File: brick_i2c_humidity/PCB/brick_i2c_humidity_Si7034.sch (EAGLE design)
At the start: 16 parts

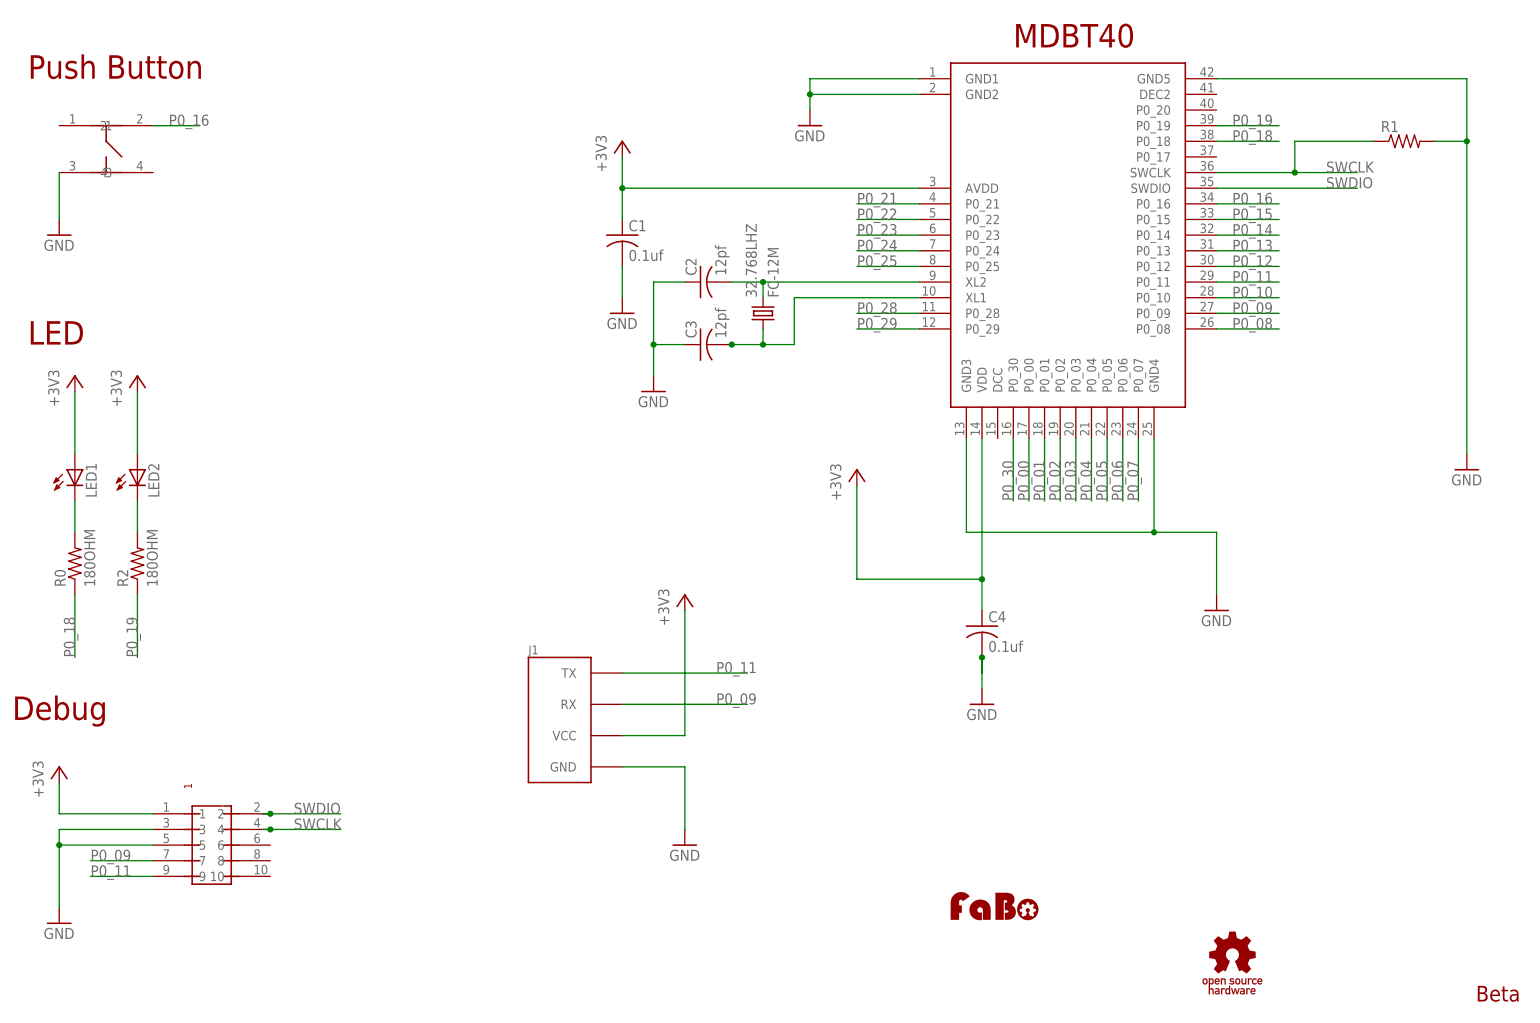
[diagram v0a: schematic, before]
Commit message: Delete unused file
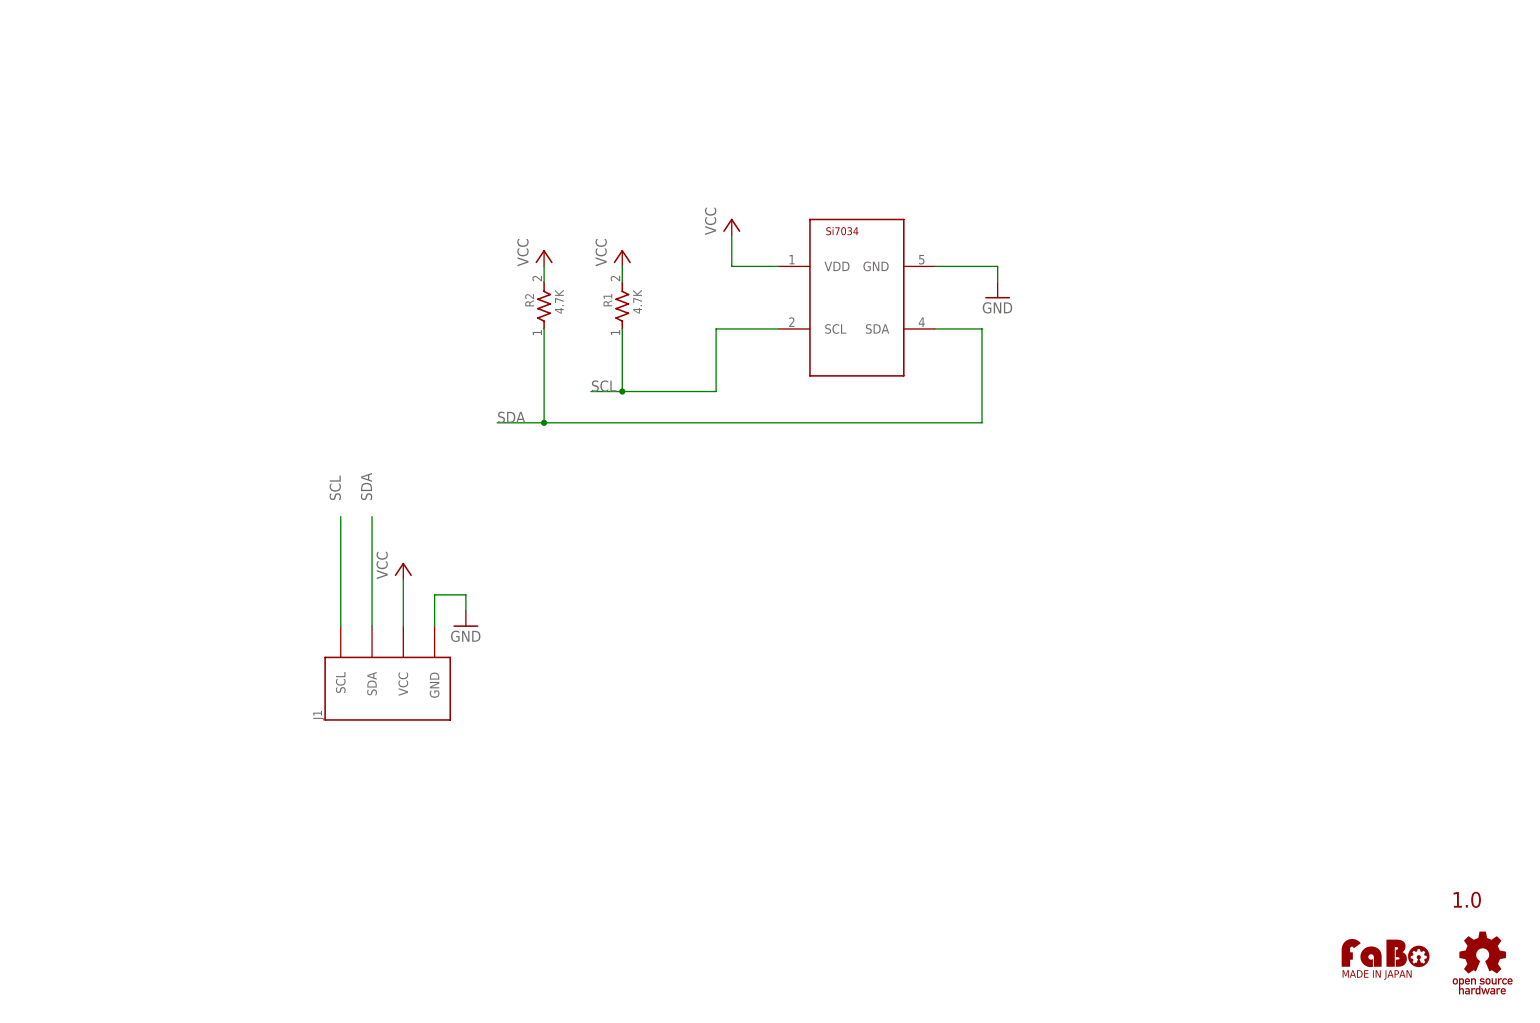
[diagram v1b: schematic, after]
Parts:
- removed 32.768LHZ: FC-12M, crystal:FC-12M
- removed C1, C4: 0.1uf, adafruit:C-USC0603
- removed C2, C3: 12pf, adafruit:C-USC0603
- removed LED1, LED2: (no value), led:LEDCHIP-LED0603
- removed R0: 180OHM, SparkFun:RESISTOR0603-RES
- removed U$1: RAYTAC-MDBT40, gclueBT:RAYTAC-MDBT40
- removed U$5: SWICTH-4P(KMR2), gclue-test:SWICTH-4P(KMR2)
- J1: device gclue:BRICK_SERIAL -> gclue:BRICK_I2C
- R1: value (none) -> 4.7K; device adafruit:R-US_R0603 -> GClue-Resistors:RESISTOR0603
- R2: value 180OHM -> 4.7K; device SparkFun:RESISTOR0603-RES -> GClue-Resistors:RESISTOR0603
- U$2: value PIN-HEADER-SMT(1.27MM)2X5 -> (none); device gclue:PIN-HEADER-SMT(1.27MM)2X5 -> FaBo:LOGO_FABO-M
- U$3: value (none) -> SILICONLABS-SI7034; device FaBo:LOGO_FABO-S -> FaBo-Mems:SILICONLABS-SI7034
- U$4: device gclue:LOGO_OSHW_T-S -> gclue:LOGO_OSHW_T-M
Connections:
- removed net +3V3: C1.1, C4.1, J1.VCC, LED1.A, LED2.A, U$1.AVDD, U$1.VDD, U$2.1
- removed net LED1: LED1.C, R0.2
- removed net N$2: LED2.C, R2.2
- removed net N$7: 32.768LHZ.2, C2.2, U$1.XL2
- removed net N$8: 32.768LHZ.1, C3.2, U$1.XL1
- removed net P0_00: U$1.P0_00
- removed net P0_01: U$1.P0_01
- removed net P0_02: U$1.P0_02
- removed net P0_03: U$1.P0_03
- removed net P0_04: U$1.P0_04
- removed net P0_05: U$1.P0_05
- removed net P0_06: U$1.P0_06
- removed net P0_07: U$1.P0_07
- removed net P0_08: U$1.P0_08
- removed net P0_09: J1.RX, U$1.P0_09, U$2.7
- removed net P0_10: U$1.P0_10
- removed net P0_11: J1.TX, U$1.P0_11, U$2.9
- removed net P0_12: U$1.P0_12
- removed net P0_13: U$1.P0_13
- removed net P0_14: U$1.P0_14
- removed net P0_15: U$1.P0_15
- removed net P0_16: U$1.P0_16, U$5.2
- removed net P0_18: R0.1, U$1.P0_18
- removed net P0_19: R2.1, U$1.P0_19
- removed net P0_21: U$1.P0_21
- removed net P0_22: U$1.P0_22
- removed net P0_23: U$1.P0_23
- removed net P0_24: U$1.P0_24
- removed net P0_25: U$1.P0_25
- removed net P0_28: U$1.P0_28
- removed net P0_29: U$1.P0_29
- removed net P0_30: U$1.P0_30
- removed net SWCLK: R1.1, U$1.SWCLK, U$2.4
- removed net SWDIO: U$1.SWDIO, U$2.2
- new net SCL: J1.SCL, R1.1, U$3.SCL
- new net SDA: J1.SDA, R2.1, U$3.SDA
- new net VCC: J1.VCC, R1.2, R2.2, U$3.VDD
- net GND: now also U$3.GND; no longer C1.2, C2.1, C3.1, C4.2, R1.2, U$1.GND1, U$1.GND2, U$1.GND3, U$1.GND4, U$1.GND5, U$2.3, U$2.5, U$5.3
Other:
- note added: "1.0"
- note removed: "Beta"
- note removed: "Debug"
- note removed: "LED"
- note removed: "MDBT40"
- note removed: "Push Button"
- moved on the sheet: J1, R1, R2

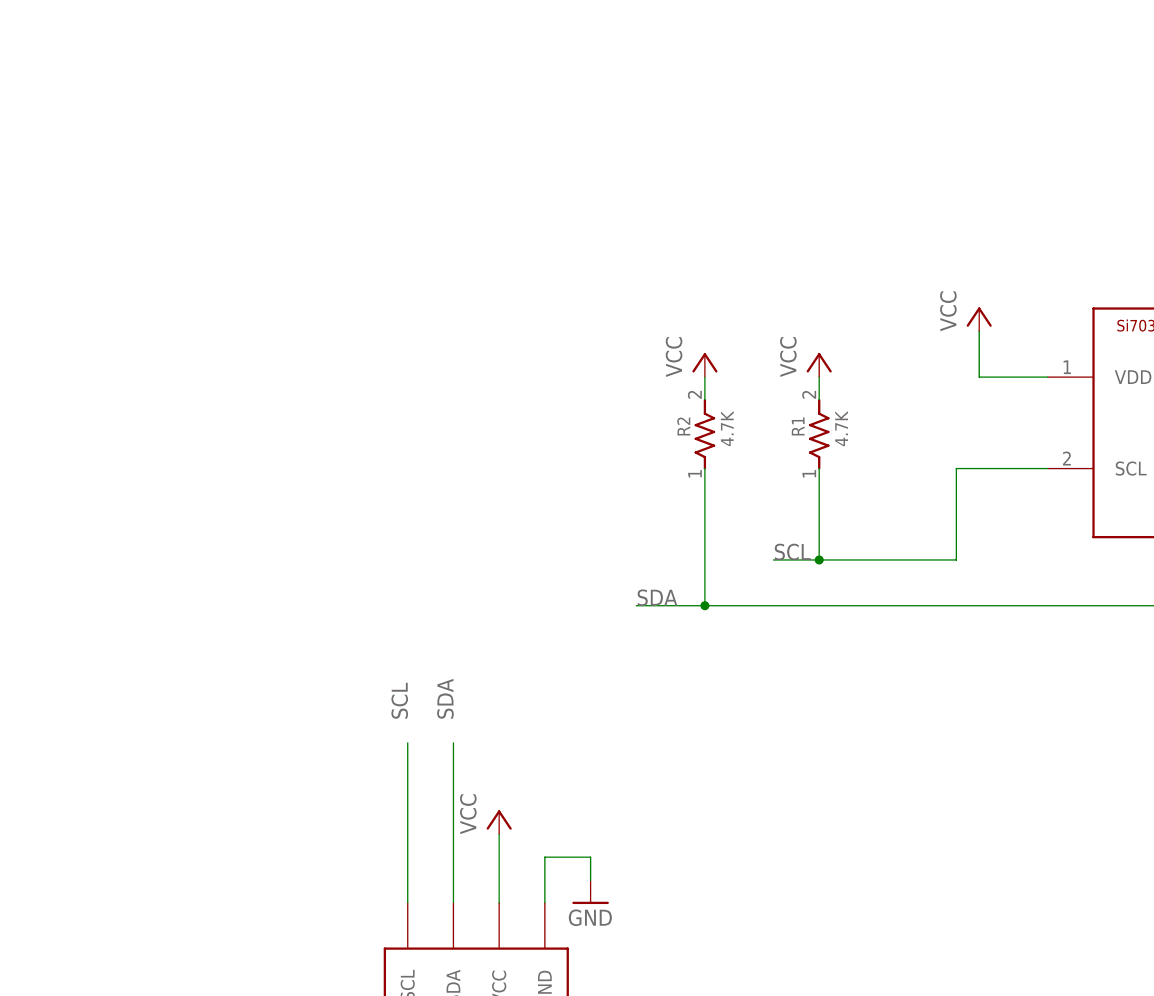
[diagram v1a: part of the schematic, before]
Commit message: Update Si7034
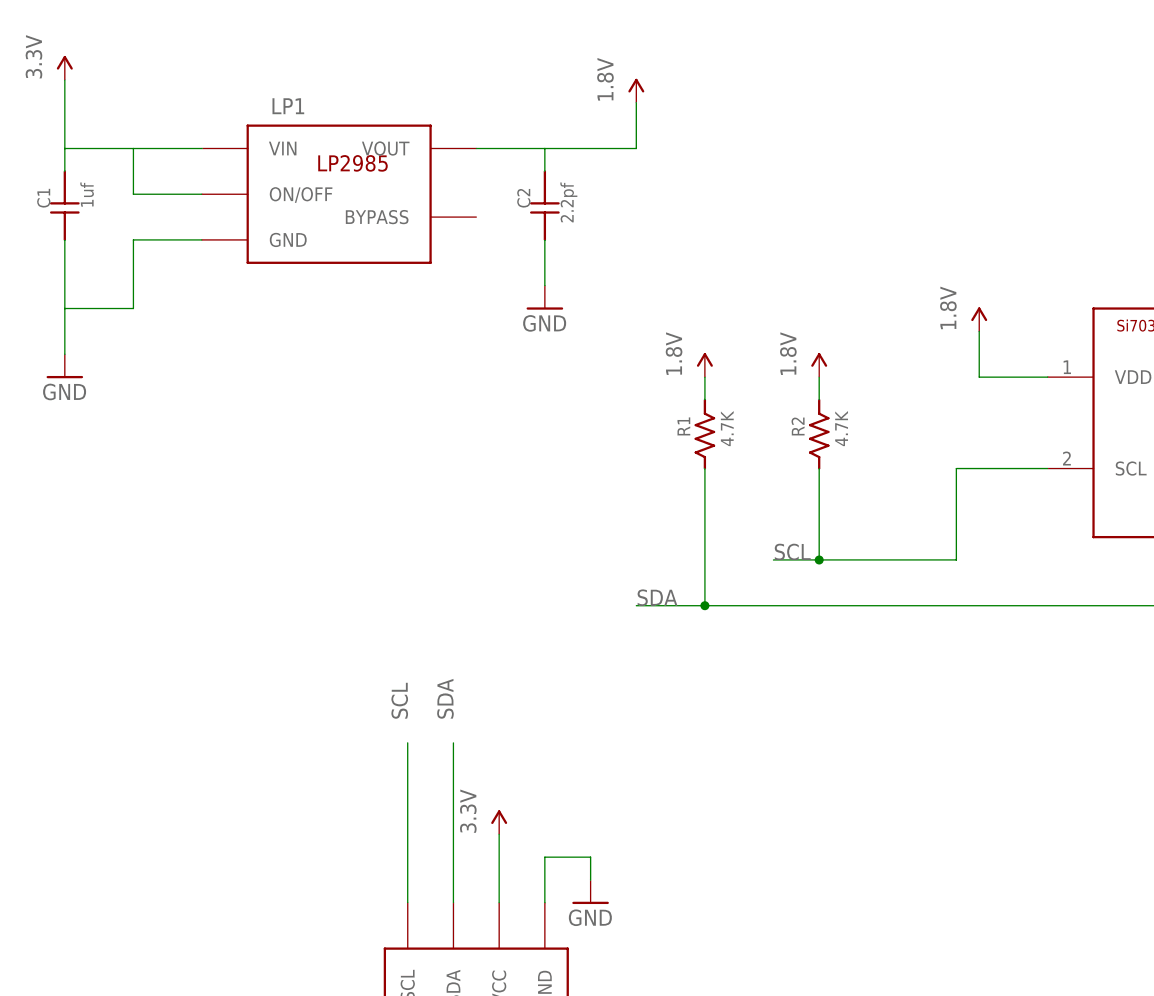
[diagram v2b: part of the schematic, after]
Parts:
- added C1: 1uf, FaBo-Capacitor:CAPACITOR0603
- added C2: 2.2pf, FaBo-Capacitor:CAPACITOR0603
- added LP1: (no value), FaBo-Supply:TI-LP2985-18DBVT
- R1, R2: device GClue-Resistors:RESISTOR0603 -> FaBo-Resistors:RESISTOR-0603
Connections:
- removed net VCC: J1.VCC, R1.2, R2.2, U$3.VDD
- new net 1.8V: C2.2, LP1.VOUT, R1.2, R2.2, U$3.VDD
- new net 3.3V: C1.2, J1.VCC, LP1.ON/OFF, LP1.VIN
- net GND: now also C1.1, C2.1, LP1.GND
- net SCL: now also R2.1; no longer R1.1
- net SDA: now also R1.1; no longer R2.1
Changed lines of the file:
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@@
 <parts>
 <part name="U$1" library="gclue" deviceset="A4L-LOC" device=""/>
-<part name="P+1" library="supply1" deviceset="VCC" device=""/>
-<part name="P+2" library="supply1" deviceset="VCC" device=""/>
-<part name="P+3" library="supply1" deviceset="VCC" device=""/>
 <part name="GND1" library="supply1" deviceset="GND" device=""/>
 <part name="GND2" library="supply1" deviceset="GND" device=""/>
 <part name="J1" library="gclue" deviceset="BRICK_I2C" device=""/>
-<part name="R2" library="GClue-Resistors" deviceset="RESISTOR" device="0603" value="4.7K"/>
-<part name="R1" library="GClue-Resistors" deviceset="RESISTOR" device="0603" value="4.7K"/>
 <part name="U$4" library="gclue" deviceset="LOGO_OSHW_T" device="-M"/>
 <part name="U$2" library="FaBo" deviceset="LOGO_FABO" device="-M"/>
 <part name="U$3" library="FaBo-Mems" deviceset="SILICONLABS-SI7034" device=""/>
-<part name="P+4" library="supply1" deviceset="VCC" device=""/>
+<part name="+1.8V1" library="FaBo-Supply" deviceset="1.8V" device=""/>
+<part name="3.3V1" library="FaBo-Supply" deviceset="3.3V" device=""/>
+<part name="+1.8V2" library="FaBo-Supply" deviceset="1.8V" device=""/>
+<part name="+1.8V3" library="FaBo-Supply" deviceset="1.8V" device=""/>
+<part name="+1.8V4" library="FaBo-Supply" deviceset="1.8V" device=""/>
+<part name="3.3V2" library="FaBo-Supply" deviceset="3.3V" device=""/>
+<part name="R1" library="FaBo-Resistors" deviceset="RESISTOR" device="-0603" value="4.7K"/>
+<part name="R2" library="FaBo-Resistors" deviceset="RESISTOR" device="-0603" value="4.7K"/>
+<part name="LP1" library="FaBo-Supply" deviceset="TI-LP2985" device="-18DBVT"/>
+<part name="GND3" library="supply1" deviceset="GND" device=""/>
+<part name="C1" library="FaBo-Capacitor" deviceset="CAPACITOR" device="0603" value="1uf"/>
+<part name="GND4" library="supply1" deviceset="GND" device=""/>
+<part name="C2" library="FaBo-Capacitor" deviceset="CAPACITOR" device="0603" value="2.2pf"/>
 </parts>
 <sheets>
@@
 <instances>
 <instance part="U$1" gate="G$1" x="0" y="0"/>
-<instance part="P+1" gate="VCC" x="73.66" y="76.2"/>
-<instance part="P+2" gate="VCC" x="109.22" y="127"/>
-<instance part="P+3" gate="VCC" x="96.52" y="127"/>
 <instance part="GND1" gate="1" x="83.82" y="66.04"/>
 <instance part="GND2" gate="1" x="170.18" y="119.38"/>
 <instance part="J1" gate="G$1" x="71.12" y="58.42" rot="R90"/>
-<instance part="R2" gate="G$1" x="96.52" y="116.84" rot="R90"/>
-<instance part="R1" gate="G$1" x="109.22" y="116.84" rot="R90"/>
 <instance part="U$4" gate="G$1" x="248.92" y="12.7"/>
 <instance part="U$2" gate="G$1" x="226.06" y="15.24"/>
 <instance part="U$3" gate="G$1" x="147.32" y="119.38"/>
-<instance part="P+4" gate="VCC" x="127" y="132.08"/>
+<instance part="+1.8V1" gate="G$1" x="88.9" y="154.94"/>
+<instance part="3.3V1" gate="G$1" x="25.4" y="157.48"/>
+<instance part="+1.8V2" gate="G$1" x="96.52" y="124.46"/>
+<instance part="+1.8V3" gate="G$1" x="109.22" y="124.46"/>
+<instance part="+1.8V4" gate="G$1" x="127" y="129.54"/>
+<instance part="3.3V2" gate="G$1" x="73.66" y="73.66"/>
+<instance part="R1" gate="G$1" x="96.52" y="116.84" rot="R90"/>
+<instance part="R2" gate="G$1" x="109.22" y="116.84" rot="R90"/>
+<instance part="LP1" gate="G$1" x="55.88" y="144.78"/>
+<instance part="GND3" gate="1" x="25.4" y="124.46"/>
+<instance part="C1" gate="G$1" x="25.4" y="142.24" rot="R90"/>
+<instance part="GND4" gate="1" x="78.74" y="132.08"/>
+<instance part="C2" gate="G$1" x="78.74" y="142.24" rot="R90"/>
 </instances>
 <busses>
@@
 <junction x="96.52" y="99.06"/>
 <label x="88.9" y="99.06" size="1.778" layer="95"/>
-<pinref part="R2" gate="G$1" pin="1"/>
 <wire x1="160.02" y1="114.3" x2="167.64" y2="114.3" width="0.1524" layer="91"/>
 <wire x1="167.64" y1="114.3" x2="167.64" y2="99.06" width="0.1524" layer="91"/>
 <pinref part="U$3" gate="G$1" pin="SDA"/>
+<pinref part="R1" gate="G$1" pin="1"/>
 </segment>
 <segment>
@@
 <label x="68.58" y="86.36" size="1.778" layer="95" rot="R90"/>
 <pinref part="J1" gate="G$1" pin="SDA"/>
-</segment>
-</net>
-<net name="VCC" class="0">
-<segment>
-<pinref part="P+2" gate="VCC" pin="VCC"/>
-<wire x1="109.22" y1="121.92" x2="109.22" y2="124.46" width="0.1524" layer="91"/>
-<pinref part="R1" gate="G$1" pin="2"/>
-</segment>
-<segment>
-<pinref part="P+3" gate="VCC" pin="VCC"/>
-<wire x1="96.52" y1="121.92" x2="96.52" y2="124.46" width="0.1524" layer="91"/>
-<pinref part="R2" gate="G$1" pin="2"/>
-</segment>
-<segment>
-<pinref part="P+1" gate="VCC" pin="VCC"/>
-<wire x1="73.66" y1="66.04" x2="73.66" y2="73.66" width="0.1524" layer="91"/>
-<pinref part="J1" gate="G$1" pin="VCC"/>
-</segment>
-<segment>
-<pinref part="U$3" gate="G$1" pin="VDD"/>
-<pinref part="P+4" gate="VCC" pin="VCC"/>
-<wire x1="134.62" y1="124.46" x2="127" y2="124.46" width="0.1524" layer="91"/>
-<wire x1="127" y1="124.46" x2="127" y2="129.54" width="0.1524" layer="91"/>
 </segment>
 </net>
@@
 <junction x="109.22" y="104.14"/>
 <label x="104.14" y="104.14" size="1.778" layer="95"/>
-<pinref part="R1" gate="G$1" pin="1"/>
 <pinref part="U$3" gate="G$1" pin="SCL"/>
+<pinref part="R2" gate="G$1" pin="1"/>
 </segment>
 <segment>
@@
 <pinref part="J1" gate="G$1" pin="GND"/>
 </segment>
+<segment>
+<pinref part="LP1" gate="G$1" pin="GND"/>
+<wire x1="40.64" y1="139.7" x2="33.02" y2="139.7" width="0.1524" layer="91"/>
+<wire x1="33.02" y1="139.7" x2="33.02" y2="132.08" width="0.1524" layer="91"/>
+<pinref part="C1" gate="G$1" pin="1"/>
+<wire x1="33.02" y1="132.08" x2="25.4" y2="132.08" width="0.1524" layer="91"/>
+<wire x1="25.4" y1="132.08" x2="25.4" y2="139.7" width="0.1524" layer="91"/>
+<pinref part="GND3" gate="1" pin="GND"/>
+<wire x1="25.4" y1="132.08" x2="25.4" y2="127" width="0.1524" layer="91"/>
+</segment>
+<segment>
+<pinref part="C2" gate="G$1" pin="1"/>
+<pinref part="GND4" gate="1" pin="GND"/>
+<wire x1="78.74" y1="139.7" x2="78.74" y2="134.62" width="0.1524" layer="91"/>
+</segment>
 </net>
+<net name="3.3V" class="0">
+<segment>
+<pinref part="3.3V1" gate="G$1" pin="3.3V"/>
+<wire x1="25.4" y1="157.48" x2="25.4" y2="149.86" width="0.1524" layer="91"/>
+<wire x1="25.4" y1="149.86" x2="33.02" y2="149.86" width="0.1524" layer="91"/>
+<pinref part="LP1" gate="G$1" pin="VIN"/>
+<pinref part="C1" gate="G$1" pin="2"/>
+<wire x1="33.02" y1="149.86" x2="40.64" y2="149.86" width="0.1524" layer="91"/>
+<wire x1="25.4" y1="149.86" x2="25.4" y2="147.32" width="0.1524" layer="91"/>
+<pinref part="LP1" gate="G$1" pin="ON/OFF"/>
+<wire x1="40.64" y1="144.78" x2="33.02" y2="144.78" width="0.1524" layer="91"/>
+<wire x1="33.02" y1="144.78" x2="33.02" y2="149.86" width="0.1524" layer="91"/>
+</segment>
+<segment>
+<wire x1="73.66" y1="66.04" x2="73.66" y2="73.66" width="0.1524" layer="91"/>
+<pinref part="J1" gate="G$1" pin="VCC"/>
+<pinref part="3.3V2" gate="G$1" pin="3.3V"/>
+</segment>
+</net>
+<net name="1.8V" class="0">
+<segment>
+<pinref part="+1.8V1" gate="G$1" pin="1.8V"/>
+<wire x1="71.12" y1="149.86" x2="78.74" y2="149.86" width="0.1524" layer="91"/>
+<wire x1="78.74" y1="149.86" x2="88.9" y2="149.86" width="0.1524" layer="91"/>
+<wire x1="88.9" y1="149.86" x2="88.9" y2="154.94" width="0.1524" layer="91"/>
+<pinref part="LP1" gate="G$1" pin="VOUT"/>
+<pinref part="C2" gate="G$1" pin="2"/>
+<wire x1="78.74" y1="147.32" x2="78.74" y2="149.86" width="0.1524" layer="91"/>
+</segment>
+<segment>
+<wire x1="96.52" y1="121.92" x2="96.52" y2="124.46" width="0.1524" layer="91"/>
+<pinref part="+1.8V2" gate="G$1" pin="1.8V"/>
+<pinref part="R1" gate="G$1" pin="2"/>
+</segment>
+<segment>
+<wire x1="109.22" y1="121.92" x2="109.22" y2="124.46" width="0.1524" layer="91"/>
+<pinref part="+1.8V3" gate="G$1" pin="1.8V"/>
+<pinref part="R2" gate="G$1" pin="2"/>
+</segment>
+<segment>
+<pinref part="U$3" gate="G$1" pin="VDD"/>
+<wire x1="134.62" y1="124.46" x2="127" y2="124.46" width="0.1524" layer="91"/>
+<wire x1="127" y1="124.46" x2="127" y2="129.54" width="0.1524" layer="91"/>
+<pinref part="+1.8V4" gate="G$1" pin="1.8V"/>
+</segment>
+</net>
